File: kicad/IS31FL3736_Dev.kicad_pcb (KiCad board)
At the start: 2 copper layers, 67.7 x 67.6 mm, 63 parts, among them J1 I/O Connector, J2 Bottom_SW_Connector, J3 Top_SW_Connector, J4 Bottom_CS_Connector, J5 Top_CS_Connector, U1 IS31FL3736

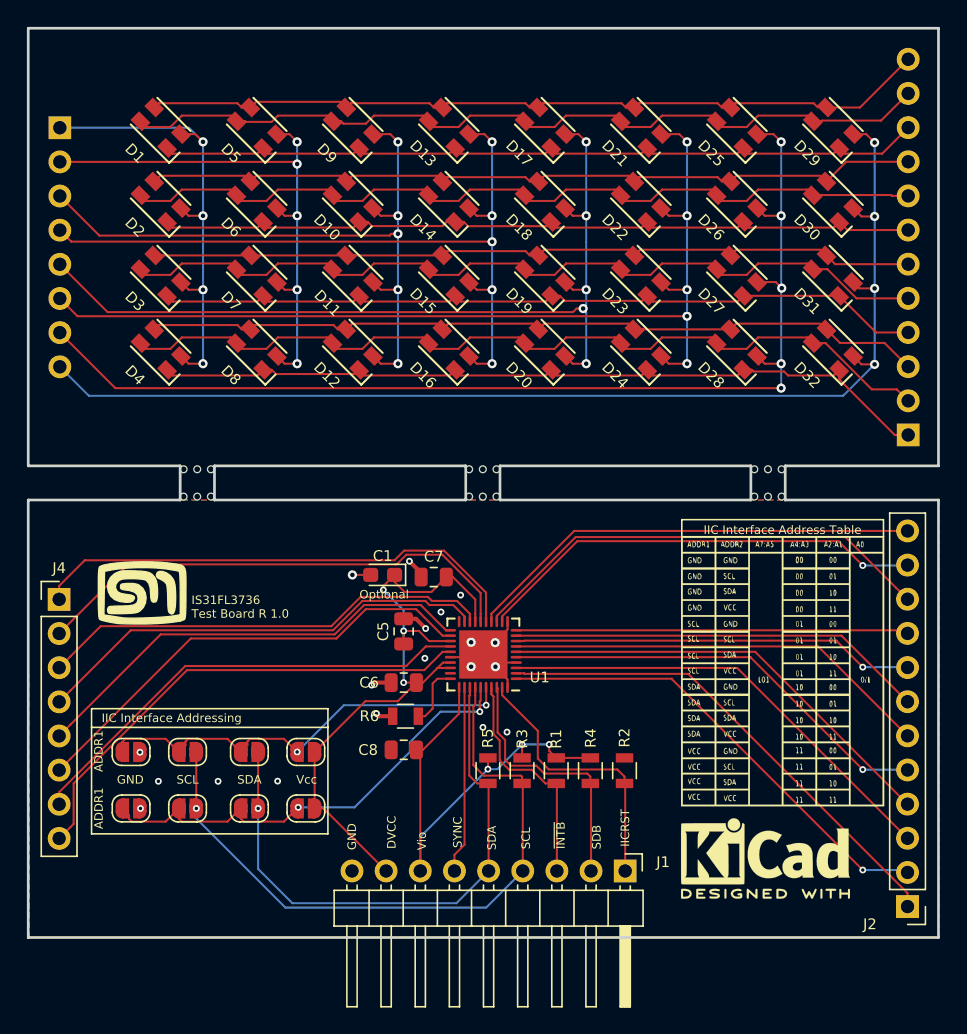
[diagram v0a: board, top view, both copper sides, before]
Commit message: Upgraded to kicad release 10.0.2
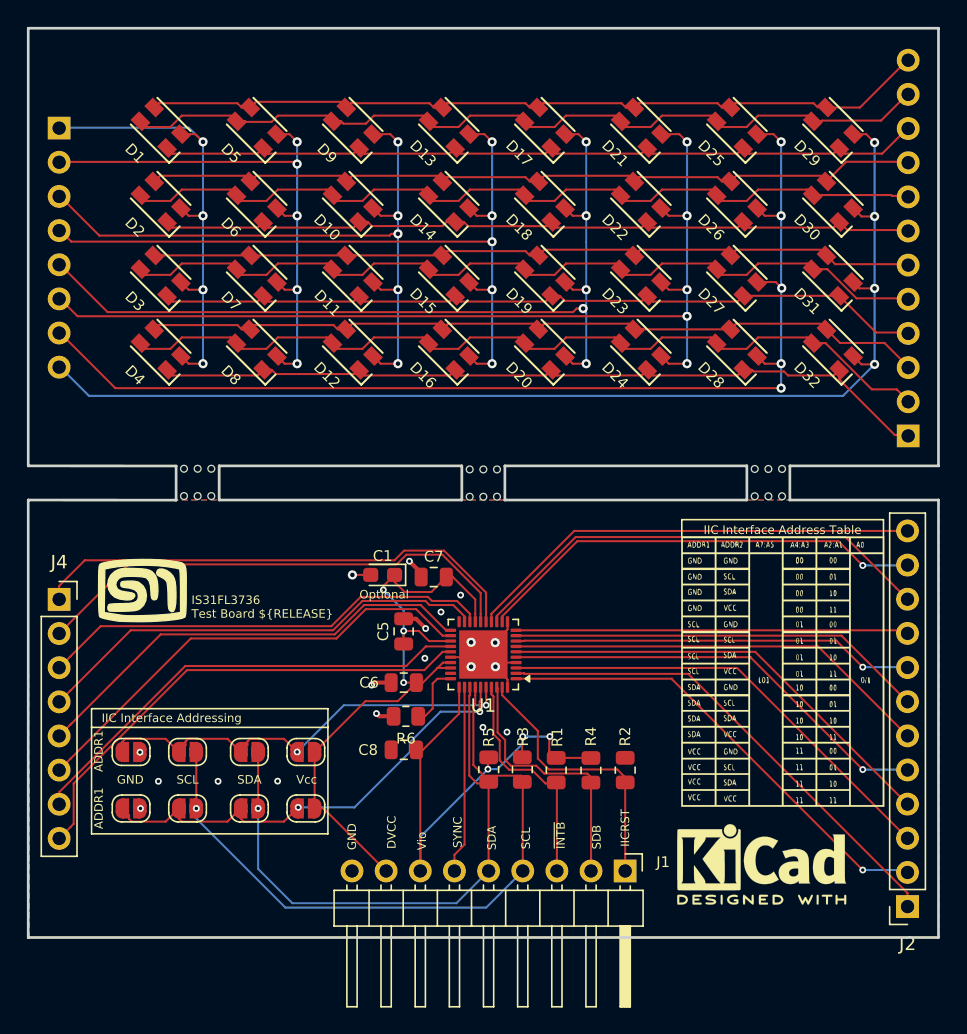
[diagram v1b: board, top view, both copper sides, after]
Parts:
- removed G***: LOGO, is31fl3736_dev:Address_Table
- removed G***: LOGO, is31fl3736_dev:MyBasic_rounded_50_1
- removed REF** (x3): MouseBites, is31fl3736_dev:MouseBites
- removed REF***: KiCad-Logo2_6mm_SilkScreen, Symbols:KiCad-Logo2_6mm_SilkScreen
- added B1: MouseBite, sjm-mech:MouseBites, F.Cu at (107.7, 67.7)
- added B2: MouseBite, sjm-mech:MouseBites, F.Cu at (128.9, 67.8)
- added B3: MouseBite, sjm-mech:MouseBites, F.Cu at (150.1, 67.7)
- added Lg1: SJM, sjm-mech:MyBasic_rounded_50_1, F.Cu at (103.5, 75.7)
- added Lg2: KiCad, Symbol:KiCad-Logo2_5mm_SilkScreen, F.Cu at (149.6, 96.1)
- added Lg3: Address Table, is31fl3736_dev:Address_Table, F.Cu at (151.2, 81.8)
- J2: footprint Pin_Headers:Pin_Header_Straight_1x12_Pitch2.54mm -> Connector_PinSocket_2.54mm:PinSocket_1x12_P2.54mm_Vertical
- J3: footprint Pin_Headers:Pin_Header_Straight_1x12_Pitch2.54mm -> Connector_PinHeader_2.54mm:PinHeader_1x12_P2.54mm_Vertical
- J4: footprint Pin_Headers:Pin_Header_Straight_1x08_Pitch2.54mm -> Connector_PinSocket_2.54mm:PinSocket_1x08_P2.54mm_Vertical
- J5: footprint Pin_Headers:Pin_Header_Straight_1x08_Pitch2.54mm -> Connector_PinHeader_2.54mm:PinHeader_1x08_P2.54mm_Vertical
- R1, R2, R3, R4, R5, R6: footprint Resistors_SMD:R_0805 -> Resistor_SMD:R_0805_2012Metric
- U1: footprint Housings_DFN_QFN:QFN-40-1EP_5x5mm_Pitch0.4mm -> Package_DFN_QFN:QFN-40-1EP_5x5mm_P0.4mm_EP3.6x3.6mm
- moved R5 0.10 mm to (129.3, 89.1)
- moved R3 0.08 mm to (131.8, 89.1)
- moved J3 0.07 mm to (160.5, 64.2)
- moved R2 0.06 mm to (139.4, 89.1)
- moved J5 0.06 mm to (97.3, 41.4)
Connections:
- net /~INT_B renamed /~{INT_B}
- net /~SDB renamed /~{SDB}
- U1 pad 20: (no net) -> unconnected-(U1-NC-Pad20)
- U1 pad 29: (no net) -> unconnected-(U1-NC-Pad29)
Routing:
- net /Vio: track 36.0 -> 37.8 mm
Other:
- outline, holes or cut-outs redrawn
- net class Default removed
- net class LED removed
- board text added: "IS31FL3736 Test Board ${RELEASE}"
- board text added: "~{INTB}"
- board text removed: "IS31FL3736 Test Board R 1.0"
- board text removed: "~INTB"
